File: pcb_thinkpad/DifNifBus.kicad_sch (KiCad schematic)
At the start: 21 parts, among them J1 700C, U10 74LVC4245, U11 74LCX07, U12 74VHCT125, U6 74LVC4245, U7 74LVC4245, U8 74LVC4245, U9 74LVC4245

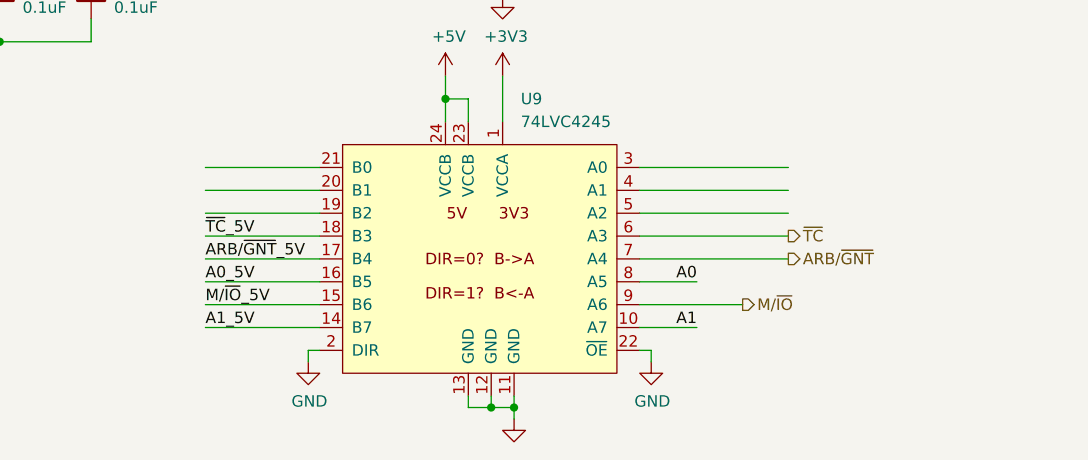
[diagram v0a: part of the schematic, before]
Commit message: Add diode OR, add clock series R
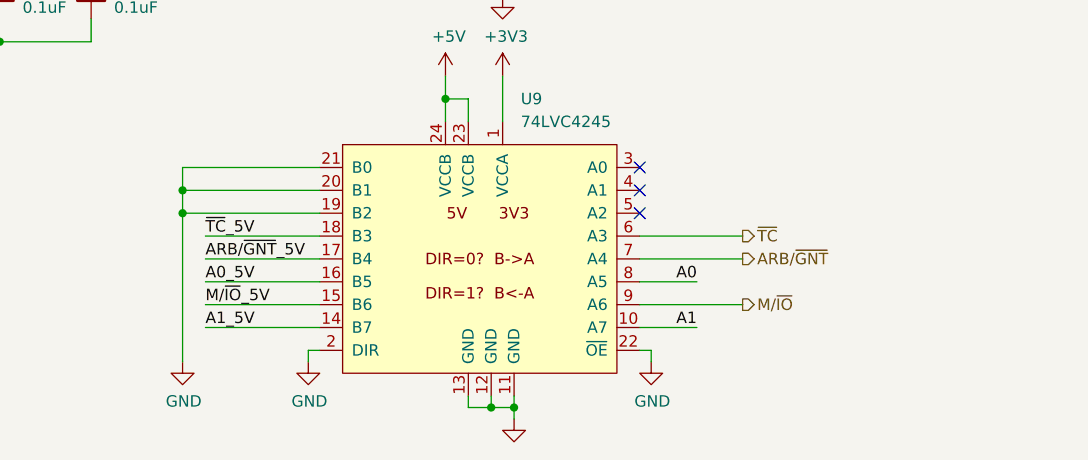
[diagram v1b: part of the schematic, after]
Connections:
- net GND: now also U9.19 (B2), U9.20 (B1), U9.21 (B0)
- no-connect marks 2 -> 5
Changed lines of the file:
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@@
   (junction (at 46.99 92.71) (diameter 0) (color 0 0 0 0)
   )
+  (junction (at 91.44 168.91) (diameter 0) (color 0 0 0 0)
+  )
   (junction (at 120.65 158.75) (diameter 0) (color 0 0 0 0)
   )
@@
   (junction (at 19.05 142.24) (diameter 0) (color 0 0 0 0)
   )
+  (junction (at 91.44 171.45) (diameter 0) (color 0 0 0 0)
+  )
   (junction (at 119.38 111.76) (diameter 0) (color 0 0 0 0)
   )
@@
   )
   (no_connect (at 48.26 64.77))
+  (no_connect (at 142.24 166.37))
+  (no_connect (at 142.24 168.91))
+  (no_connect (at 142.24 171.45))
   (no_connect (at 187.96 128.27))
   (bus_entry (at -39.37 185.42) (size 2.54 -2.54)
@@
     (stroke (width 0) (type default) (color 0 0 0 0))
   )
-  (wire (pts (xy 142.24 171.45) (xy 158.75 171.45))
-    (stroke (width 0) (type default) (color 0 0 0 0))
-  )
   (wire (pts (xy 60.96 97.79) (xy 73.66 97.79))
     (stroke (width 0) (type default) (color 0 0 0 0))
@@
     (stroke (width 0) (type default) (color 0 0 0 0))
   )
-  (wire (pts (xy 93.98 168.91) (xy 106.68 168.91))
+  (wire (pts (xy 91.44 168.91) (xy 106.68 168.91))
     (stroke (width 0) (type default) (color 0 0 0 0))
   )
@@
     (stroke (width 0) (type default) (color 0 0 0 0))
   )
-  (wire (pts (xy 142.24 176.53) (xy 158.75 176.53))
+  (wire (pts (xy 142.24 176.53) (xy 153.67 176.53))
     (stroke (width 0) (type default) (color 0 0 0 0))
   )
@@
     (stroke (width 0) (type default) (color 0 0 0 0))
   )
-  (wire (pts (xy 142.24 166.37) (xy 158.75 166.37))
-    (stroke (width 0) (type default) (color 0 0 0 0))
-  )
   (wire (pts (xy 35.56 115.57) (xy 48.26 115.57))
     (stroke (width 0) (type default) (color 0 0 0 0))
@@
     (stroke (width 0) (type default) (color 0 0 0 0))
   )
+  (wire (pts (xy 91.44 168.91) (xy 91.44 171.45))
+    (stroke (width 0) (type default) (color 0 0 0 0))
+  )
   (bus (pts (xy 154.94 83.82) (xy 154.94 81.28))
     (stroke (width 0) (type default) (color 0 0 0 0))
   )
-  (wire (pts (xy 142.24 168.91) (xy 158.75 168.91))
-    (stroke (width 0) (type default) (color 0 0 0 0))
-  )
   (wire (pts (xy 175.26 109.22) (xy 187.96 109.22))
     (stroke (width 0) (type default) (color 0 0 0 0))
@@
     (stroke (width 0) (type default) (color 0 0 0 0))
   )
-  (wire (pts (xy 93.98 166.37) (xy 106.68 166.37))
+  (wire (pts (xy 91.44 166.37) (xy 106.68 166.37))
     (stroke (width 0) (type default) (color 0 0 0 0))
   )
@@
     (stroke (width 0) (type default) (color 0 0 0 0))
   )
-  (wire (pts (xy 142.24 173.99) (xy 158.75 173.99))
+  (wire (pts (xy 142.24 173.99) (xy 153.67 173.99))
     (stroke (width 0) (type default) (color 0 0 0 0))
   )
@@
     (stroke (width 0) (type default) (color 0 0 0 0))
   )
+  (wire (pts (xy 91.44 171.45) (xy 91.44 187.96))
+    (stroke (width 0) (type default) (color 0 0 0 0))
+  )
   (wire (pts (xy 194.31 24.13) (xy 194.31 22.86))
     (stroke (width 0) (type default) (color 0 0 0 0))
@@
     (stroke (width 0) (type default) (color 0 0 0 0))
   )
-  (wire (pts (xy 93.98 171.45) (xy 106.68 171.45))
+  (wire (pts (xy 91.44 171.45) (xy 106.68 171.45))
     (stroke (width 0) (type default) (color 0 0 0 0))
   )
@@
     (stroke (width 0) (type default) (color 0 0 0 0))
   )
+  (wire (pts (xy 91.44 166.37) (xy 91.44 168.91))
+    (stroke (width 0) (type default) (color 0 0 0 0))
+  )
   (wire (pts (xy 121.92 111.76) (xy 119.38 111.76))
     (stroke (width 0) (type default) (color 0 0 0 0))
@@
     (effects (font (size 1.27 1.27)) (justify left))
   )
-  (hierarchical_label "~{TC}" (shape output) (at 158.75 173.99 0)
+  (hierarchical_label "~{TC}" (shape output) (at 153.67 173.99 0)
     (effects (font (size 1.27 1.27)) (justify left))
   )
@@
     (effects (font (size 1.27 1.27)) (justify left))
   )
-  (hierarchical_label "ARB{slash}~{GNT}" (shape output) (at 158.75 176.53 0)
+  (hierarchical_label "ARB{slash}~{GNT}" (shape output) (at 153.67 176.53 0)
     (effects (font (size 1.27 1.27)) (justify left))
   )
@@
     (pin "7")
   )
+  (symbol (lib_id "power:GND") (at 91.44 187.96 0) (unit 1)
+    (in_bom yes) (on_board yes)
+    (property "Reference" "#PWR0116" (id 0) (at 91.44 194.31 0)
+      (effects (font (size 1.27 1.27)) hide)
+    )
+    (property "Value" "GND" (id 1) (at 91.567 192.3542 0))
+    (property "Footprint" "" (id 2) (at 91.44 187.96 0)
+      (effects (font (size 1.27 1.27)) hide)
+    )
+    (property "Datasheet" "" (id 3) (at 91.44 187.96 0)
+      (effects (font (size 1.27 1.27)) hide)
+    )
+    (pin "1")
+  )
   (symbol (lib_id "Device:C_Small") (at 60.96 173.99 0) (unit 1)
